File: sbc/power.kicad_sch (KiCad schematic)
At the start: 23 parts, among them J9 Power-Connector, U14 AP22814AW5

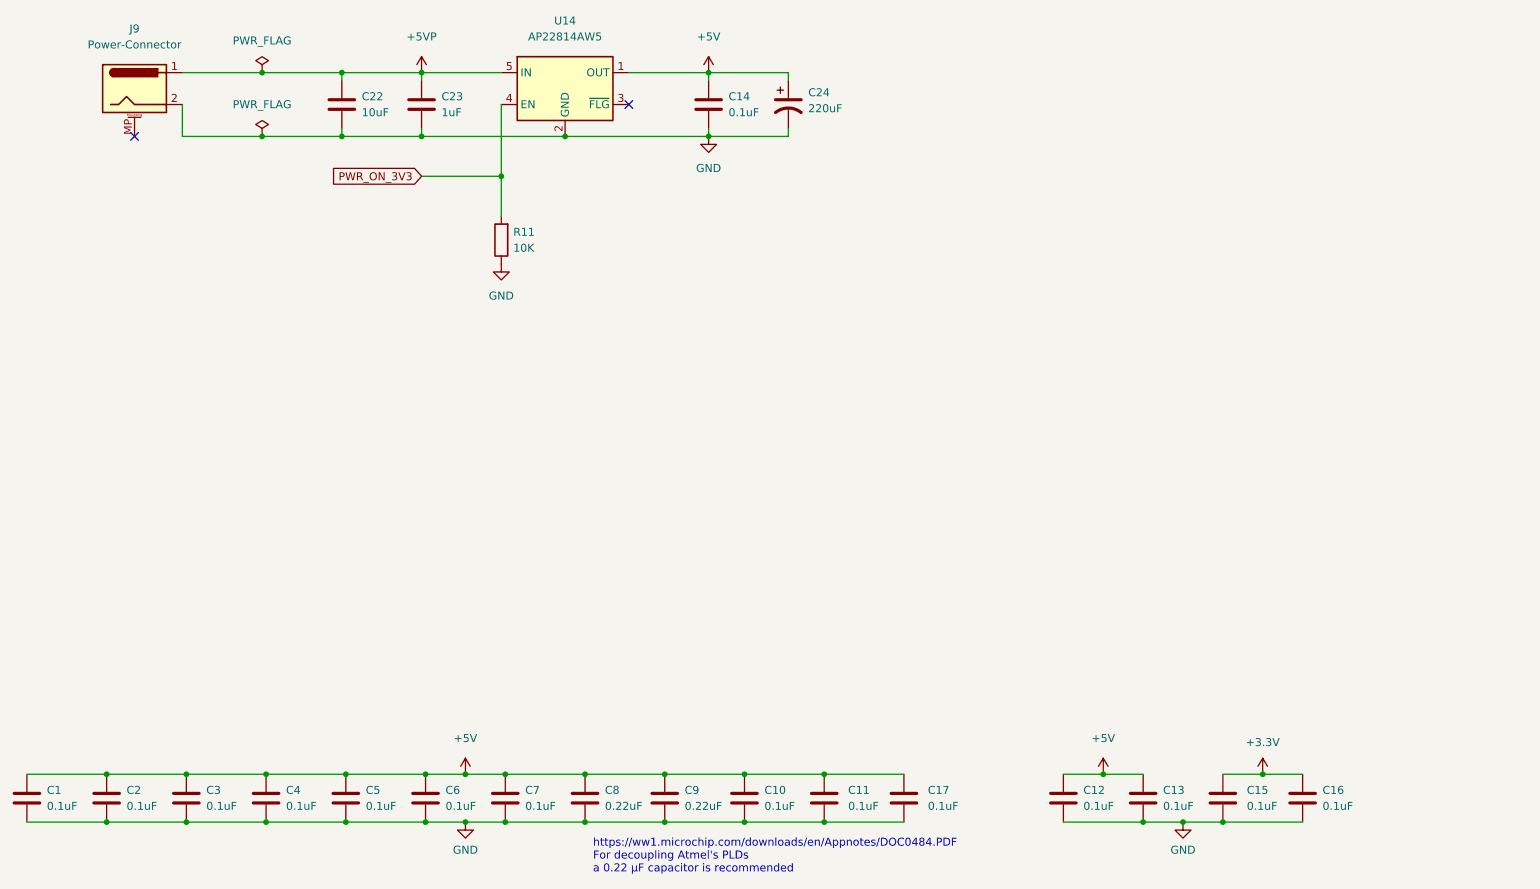
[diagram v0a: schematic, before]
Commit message: SBC v1.1
PCB fixes/changes:

  - Permanently power voltage translators
  - Conservatively specified a slower SRAM (the previous/faster SRAM does actually work fine)
  - RMU: Speculatively provided unbuffered PHI0 input and OE output (not actually needed)
  - Add pullups to open drain GTIA outputs
  - Plot selected values on silk screen
  - Accommodate KiCad 7 upgrade

- PLD changes:
  - Fix AMU logic
  - Fix RMU (unbuffered PHI0 and OE output not needed)

- QTPY firmware:
  - add soft power on/off support (Ctrl-F12)
  - reflects switched power and usb state in the neopixel
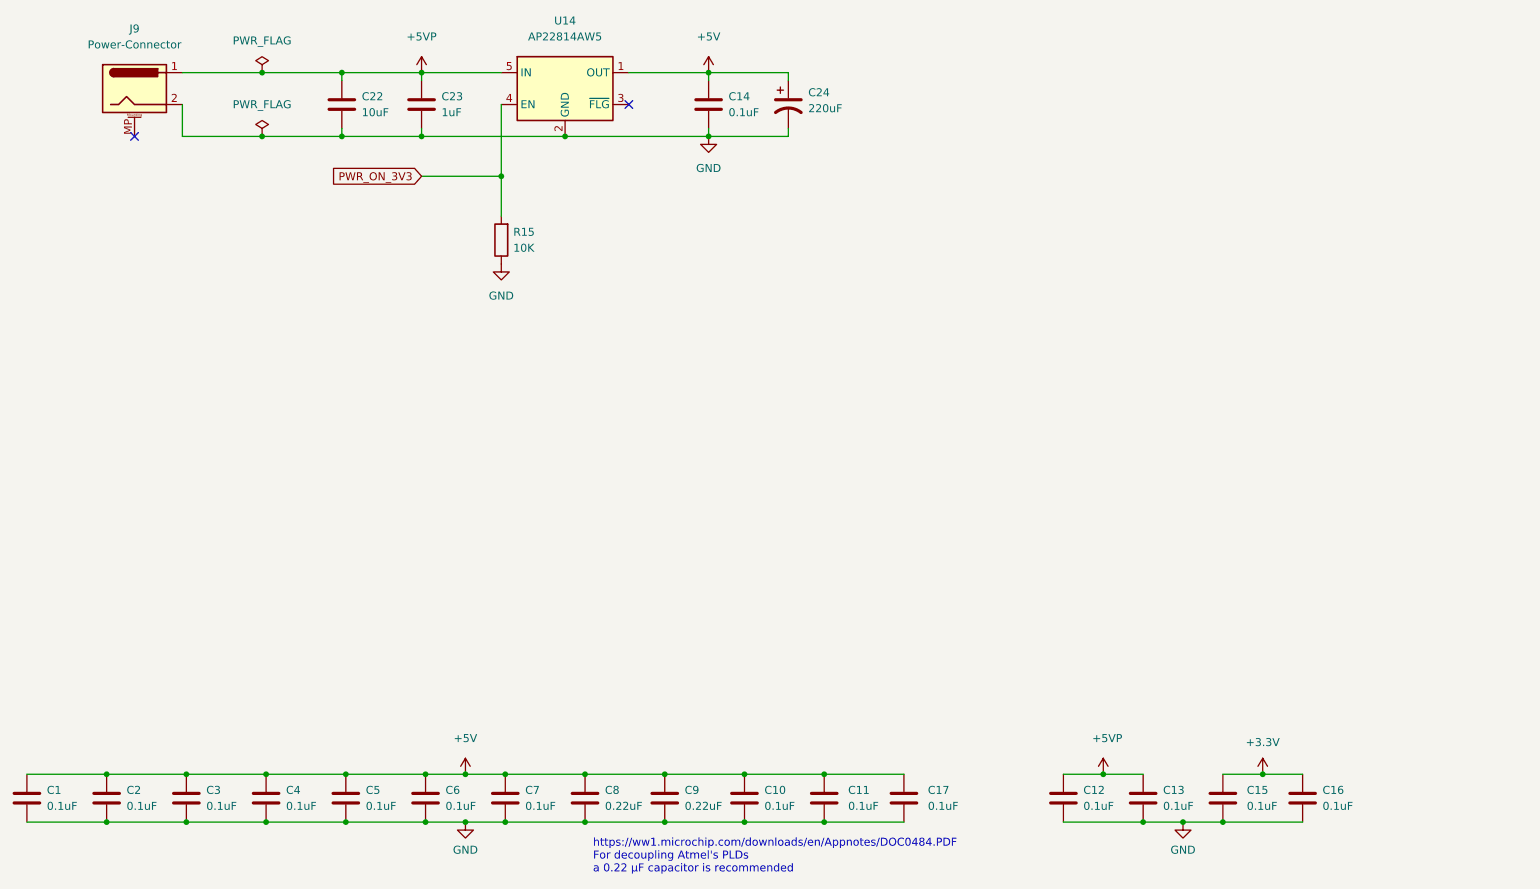
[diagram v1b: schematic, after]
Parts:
- renumbered R11 to R15
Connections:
- net +5V: no longer C12.1, C13.1
- net +5VP: now also C12.1, C13.1
- net +3V3 renamed +3.3V

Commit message: SBC v1.2
SBC fixes/changes:

  - S-Video:
    - Fix S-Video footprint (Y and C swapped, and GNDs swapped) and adapt schematic to match
    - Wire S-Video grounds to AVA header instead of directly to (digital) GND
  - Audio:
    - Wire Audio-Out ground to AVA header
    - Drop SIO audio
    - Pullup open drain pokey audio
  - AMU/RMU:
    - Connect ROM and RAM OE to GND
    - Reserve AMU pin for "IO"
    - Reserve RMU pin for "antic" (registered halt)
    - Support for separate Antic banking (clock RMU with /phi2)
    - Supoprt 130XE and 320XE (compy)
  - Add the option for a resistor between OSC, PHI0 buffer and PHI2 buffer (to reduce over/under-shoot)
  - Invert CA2 (a PNP transistor on the Atari 800 XL inverts this signal)

Additions:

  - SBC Audio/Video board
  - SBC Case
  - SBC SD board

Stylize the complete system as "SFF 320XE".
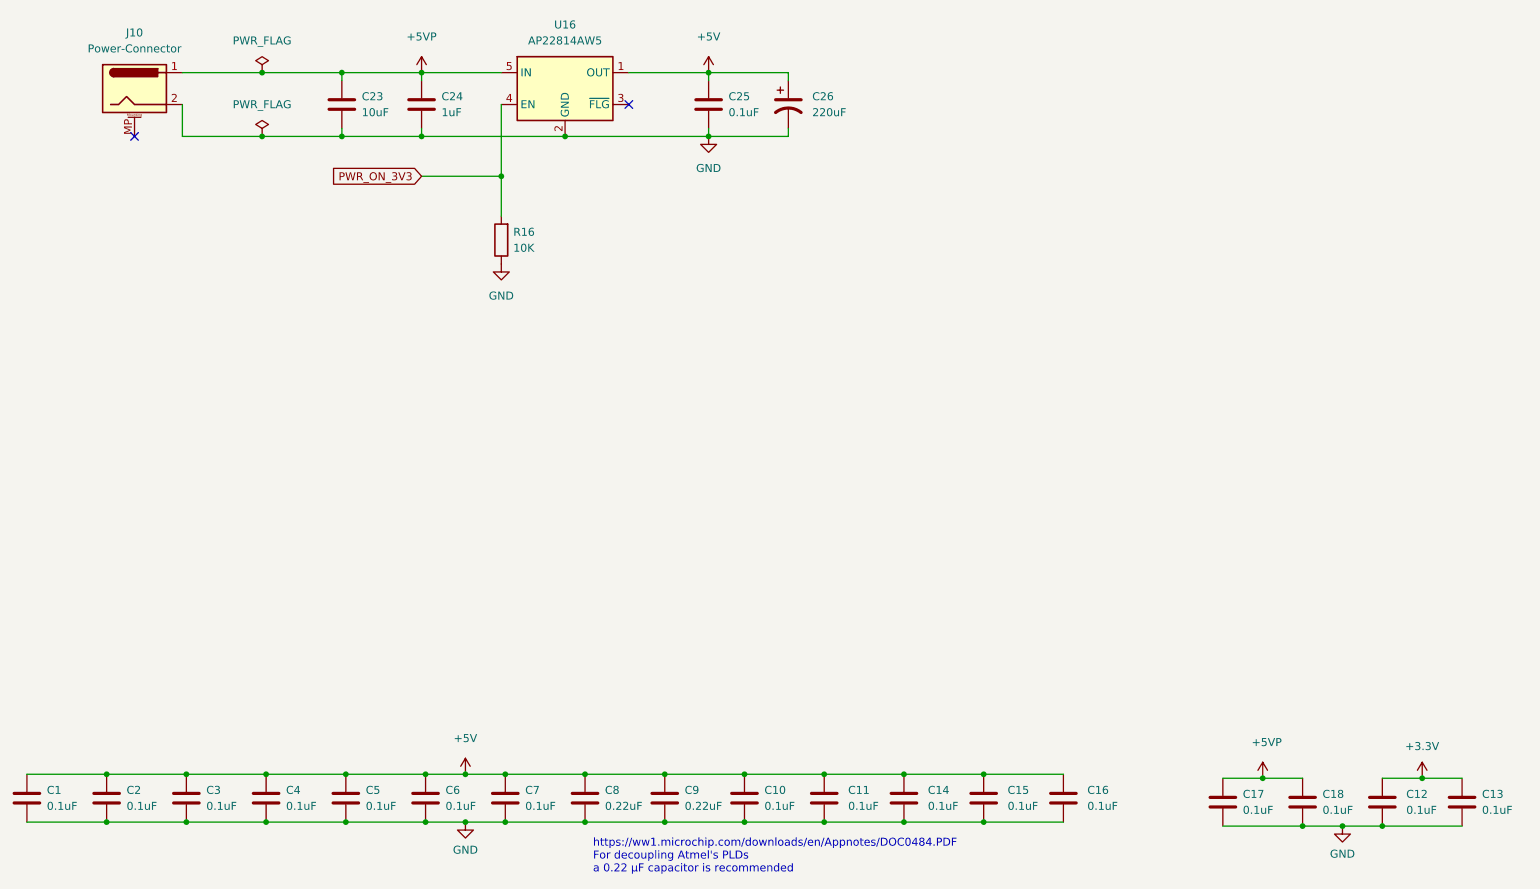
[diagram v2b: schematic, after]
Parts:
- added C14, C15: 0.1uF, Capacitor_SMD:C_0805_2012Metric_Pad1.18x1.45mm_HandSolder, symbol Device:C
- renumbered C15 to C12, C16 to C13, C17 to C16, C12 to C17, C13 to C18, C22 to C23, C23 to C24, C14 to C25, C24 to C26, J9 to J10, R15 to R16, U14 to U16
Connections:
- net +5V: now also C14.1, C15.1
- net GND: now also C14.2, C15.2
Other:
- moved on the sheet: C12, C13, C16, C17, C18

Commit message: SBC v1.3
Motherboard updates:

  - KiCad 9 upgrade
  - USB-C power connector
  - Replace EOL resistor packs with discrete SMD resistors
  - Power/enable voltage translators from switched 5V
  - Fix motor signal pullup
  - Eliminate loop in phi2 traces
  - Thicker clock signal traces

SD card adapter updates:

  - KiCad 9 upgrade
  - Power/enable voltage translator from switched 5V and the eliminate unnecessary SIO pullups

Audio/Video adapter updates:

  - KiCad 9 upgrade
  - No functional changes, gerbers not regenerated, cleaned up bom
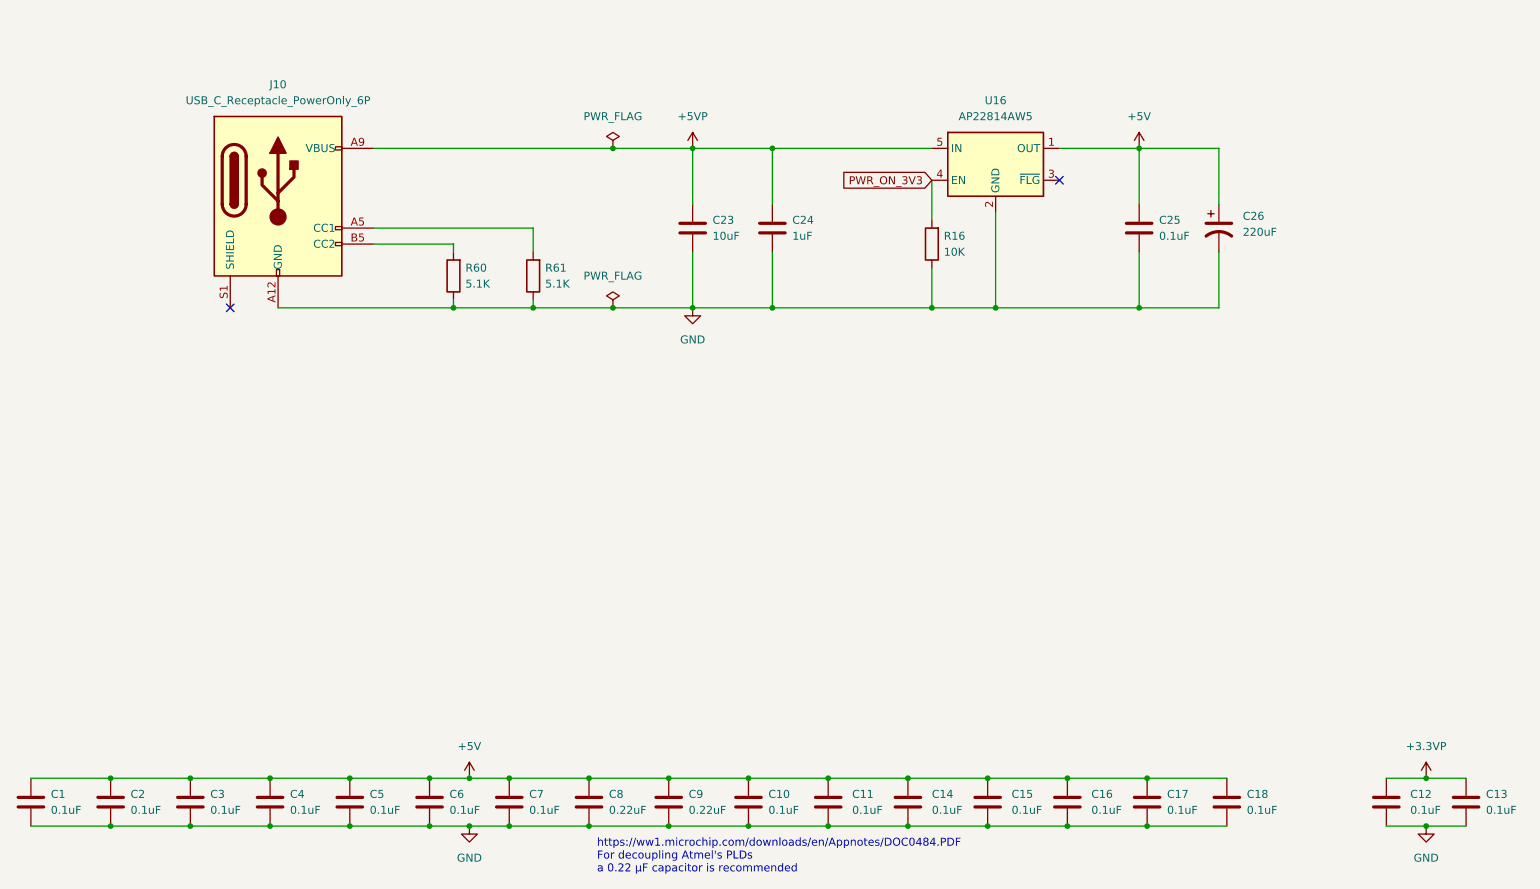
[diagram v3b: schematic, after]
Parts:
- removed J10: Power-Connector, Connector_BarrelJack:BarrelJack_CUI_PJ-063AH_Horizontal, symbol Connector:Barrel_Jack_MountingPin
- added J10: USB_C_Receptacle_PowerOnly_6P, Connector_USB:USB_C_Receptacle_GCT_USB4125-xx-x_6P_TopMnt_Horizontal, symbol Connector:USB_C_Receptacle_PowerOnly_6P
- added R60, R61: 5.1K, Resistor_SMD:R_0805_2012Metric_Pad1.20x1.40mm_HandSolder, symbol Device:R
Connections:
- net +5V: now also C17.1, C18.1
- net +5VP: now also J10.A9 (VBUS), J10.B9 (VBUS); no longer C17.1, C18.1
- net GND: now also J10.A12 (GND), J10.B12 (GND), R60.1, R61.1
- net +3.3V renamed +3.3VP
- new net: J10.A5 (CC1), R61.2
- new net: J10.B5 (CC2), R60.2
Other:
- moved on the sheet: C1, C10, C11, C12, C13, C14, C15, C16, C17, C18, C2, C23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
